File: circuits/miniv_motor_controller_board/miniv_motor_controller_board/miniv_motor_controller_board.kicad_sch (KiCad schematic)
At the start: 5 parts, among them U1 Teensy4.1, U2 NSL-32

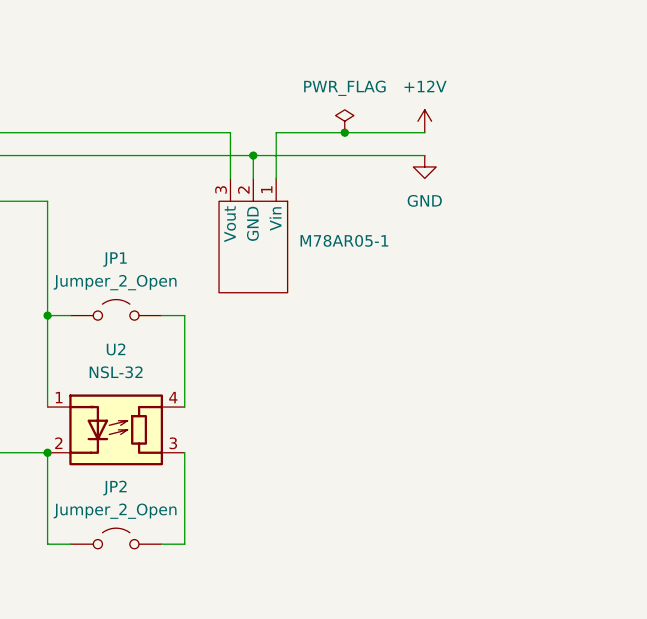
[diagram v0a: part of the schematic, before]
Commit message: add connectors
Signed-off-by: Masaya Kataoka <ms.kataoka@gmail.com>
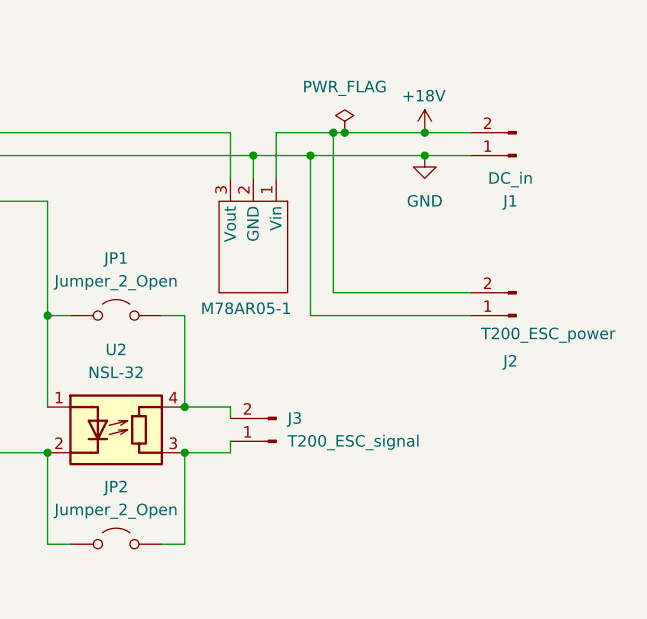
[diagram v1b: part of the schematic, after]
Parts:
- added J1: DC_in, symbol Connector:Conn_01x02_Pin
- added J2: T200_ESC_power, symbol Connector:Conn_01x02_Pin
- added J3: T200_ESC_signal, symbol Connector:Conn_01x02_Pin
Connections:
- net GND: now also J1.1 (Pin_1), J2.1 (Pin_1)
- net at JP1.2 (B), U2.4 (R): now also J3.2 (Pin_2)
- net at JP2.2 (B), U2.3 (R): now also J3.1 (Pin_1)
- net +12V renamed +18V
- net +18V: now also J1.2 (Pin_2), J2.2 (Pin_2)

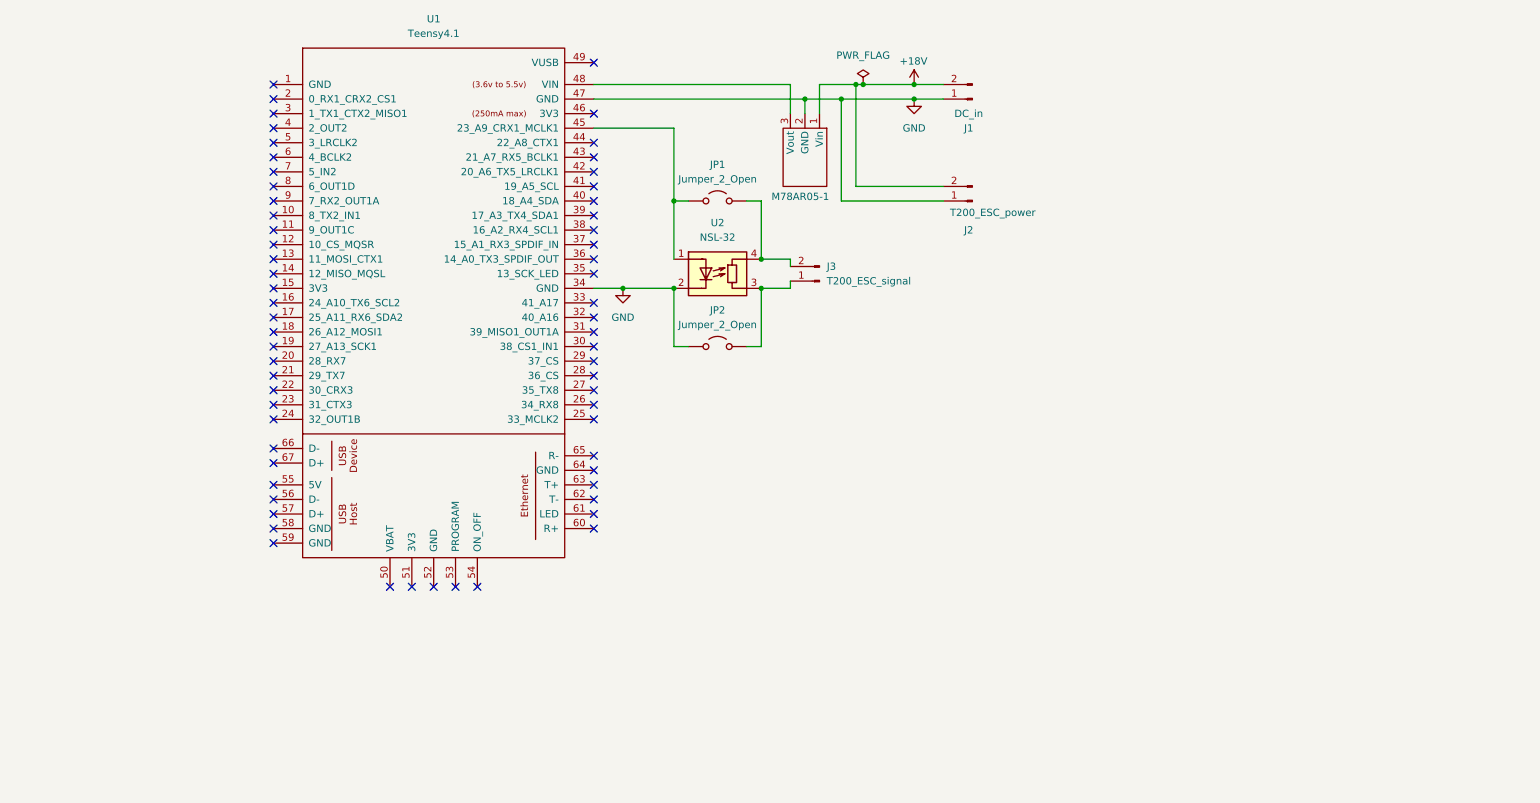
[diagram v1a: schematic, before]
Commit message: add some footprint
Signed-off-by: Masaya Kataoka <ms.kataoka@gmail.com>
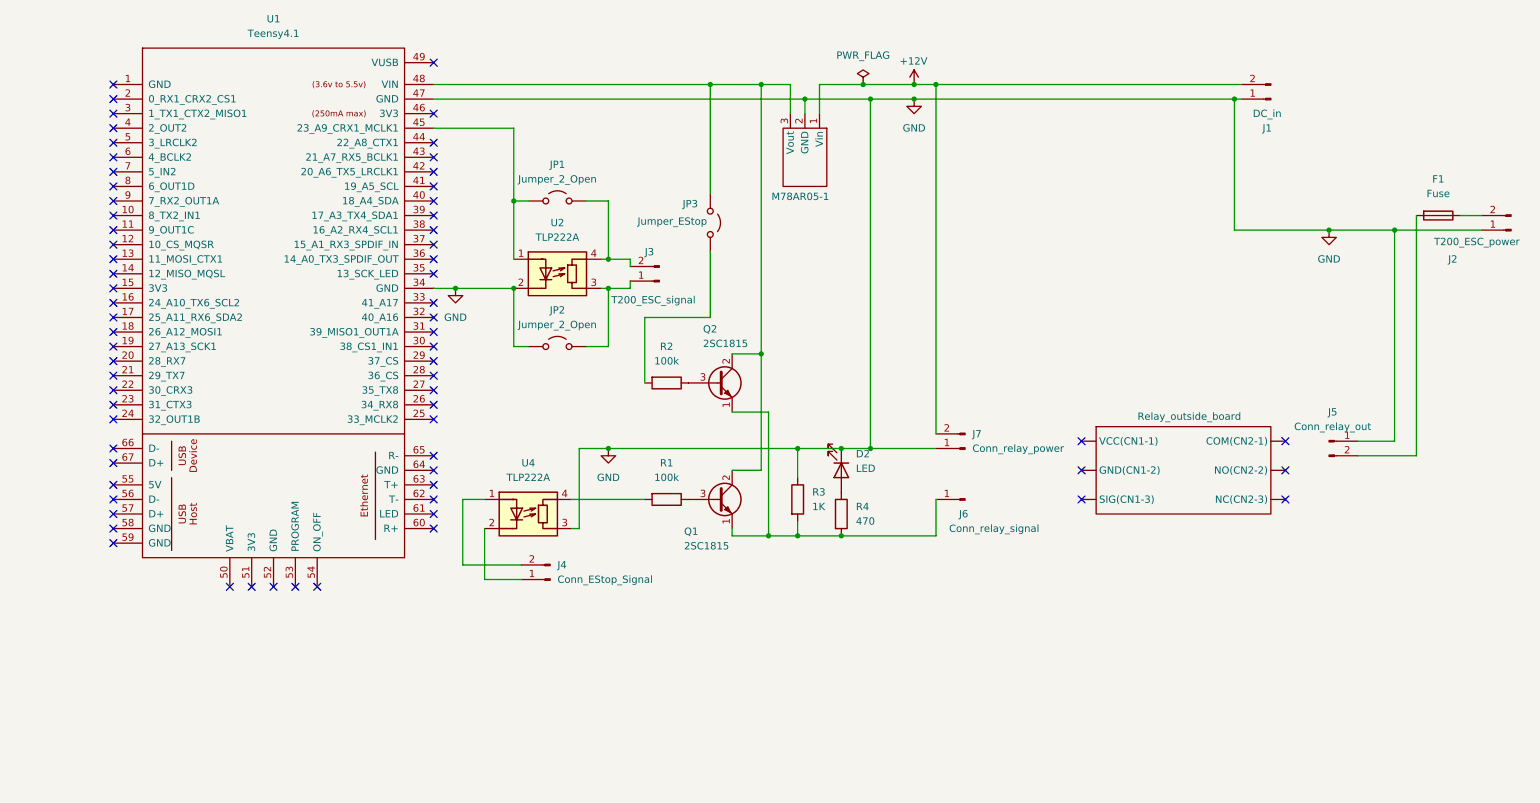
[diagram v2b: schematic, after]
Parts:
- added D2: LED, LED_THT:LED_D3.0mm, symbol Device:LED
- added F1: Fuse, 3557-15:3557-15, symbol Device:Fuse
- added J4: Conn_EStop_Signal, Connector_AMASS:AMASS_XT30PW-F_1x02_P2.50mm_Horizontal, symbol Connector:Conn_01x02_Pin
- added J5: Conn_relay_out, symbol Connector:Conn_01x02_Pin
- added J6: Conn_relay_signal, symbol Connector:Conn_01x01_Pin
- added J7: Conn_relay_power, symbol Connector:Conn_01x02_Pin
- added JP3: Jumper_EStop, Connector_PinHeader_2.54mm:PinHeader_1x02_P2.54mm_Vertical, symbol Jumper:Jumper_2_Open
- added Q1, Q2: 2SC1815, Package_TO_SOT_THT:TO-92_Inline, symbol Transistor_BJT:2SC1815
- added R1, R2: 100k, Resistor_THT:R_Axial_DIN0207_L6.3mm_D2.5mm_P10.16mm_Horizontal, symbol Device:R
- added R3: 1K, Resistor_THT:R_Axial_DIN0207_L6.3mm_D2.5mm_P10.16mm_Horizontal, symbol Device:R
- added R4: 470, Resistor_THT:R_Axial_DIN0207_L6.3mm_D2.5mm_P10.16mm_Horizontal, symbol Device:R
- added Relay_outside_board: ~, symbol AE-RELAY953B-12V:AE-RELAY953B-12V
- added U4: TLP222A, Package_DIP:DIP-4_W7.62mm, symbol Isolator:NSL-32
- J1, J2: footprint (none) -> Connector_AMASS:AMASS_XT30PW-F_1x02_P2.50mm_Horizontal
- JP1, JP2: footprint (none) -> Connector_PinHeader_2.54mm:PinHeader_1x02_P2.54mm_Vertical
- U1: footprint (none) -> Teensy:Teensy41
- U2: value NSL-32 -> TLP222A; footprint OptoDevice:Luna_NSL-32 -> Package_DIP:DIP-4_W7.62mm
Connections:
- net GND: now also D2.1 (K), J5.1 (Pin_1), J7.1 (Pin_1), R3.1, U4.3 (R)
- net at M78AR05-1.3 (Vout), U1.48 (VIN): now also JP3.1 (A), Q1.2 (C), Q2.2 (C)
- net +18V renamed +12V
- net +12V: now also J7.2 (Pin_2); no longer J2.2 (Pin_2)
- new net: J6.1 (Pin_1), Q1.1 (E), Q2.1 (E), R3.2, R4.2
- new net: D2.2 (A), R4.1
- new net: Q2.3 (B), R2.1
- new net: JP3.2 (B), R2.2
- new net: F1.1, J2.2 (Pin_2)
- new net: F1.2, J5.2 (Pin_2)
- new net: Q1.3 (B), R1.1
- new net: J4.1 (Pin_1), U4.2 (K)
- new net: J4.2 (Pin_2), U4.1 (A)
- new net: R1.2, U4.4 (R)
- no-connect marks 63 -> 69
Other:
- moved on the sheet: J1, J2, J3, JP1, JP2, U1, U2

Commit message: update connection
Signed-off-by: Masaya Kataoka <ms.kataoka@gmail.com>
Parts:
- removed J5: Conn_relay_out, symbol Connector:Conn_01x02_Pin
- removed J6: Conn_relay_signal, symbol Connector:Conn_01x01_Pin
- removed J7: Conn_relay_power, symbol Connector:Conn_01x02_Pin
- removed U2, U4: TLP222A, Package_DIP:DIP-4_W7.62mm, symbol Isolator:NSL-32
- added JP4, JP5, JP6: Jumper_2_Bridged, Connector_Wire:SolderWire-0.1sqmm_1x01_D0.4mm_OD1mm, symbol Jumper:Jumper_2_Bridged
- added JP7, JP8: Jumper_2_Bridged, Connector_Wire:SolderWire-0.5sqmm_1x01_D0.9mm_OD2.1mm, symbol Jumper:Jumper_2_Bridged
- added U2, U3: TLP222A, Package_DIP:DIP-4_W7.62mm, symbol Relay_SolidState:TLP222A
- renumbered Relay_outside_board to U4
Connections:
- net +12V: now also JP6.1 (A)
- net GND: now also JP5.1 (A), JP8.2 (B), U2.2
- net at JP1.1 (A), U1.45 (23_A9_CRX1_MCLK1): now also U2.1
- net at J3.2 (Pin_2), JP1.2 (B): now also U2.4
- net at Q1.1 (E), Q2.1 (E), R3.2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: now also JP4.1 (A)
- net at JP3.2 (B), R2.2: now also U3.4
- net at J3.1 (Pin_1), JP2.2 (B): now also U2.3
- net at F1.2: now also JP7.2 (B)
- net at U4. (VCC(CN1-1)): now also JP7.1 (A)
- net at J4.1 (Pin_1): now also U3.2
- net at J4.2 (Pin_2): now also U3.1
- net at R1.2: now also U3.3
- new net: JP8.1 (A), U4. (VCC(CN1-1))
- new net: JP5.2 (B), U4. (VCC(CN1-1))
- new net: JP6.2 (B), U4. (VCC(CN1-1))
- new net: JP4.2 (B), U4. (VCC(CN1-1))
- no-connect marks 69 -> 64
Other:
- moved on the sheet: U4

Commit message: modify resister
Signed-off-by: Masaya Kataoka <ms.kataoka@gmail.com>
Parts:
- removed JP2: Jumper_2_Open, Connector_PinHeader_2.54mm:PinHeader_1x02_P2.54mm_Vertical, symbol Jumper:Jumper_2_Open
- added R5: 390, Resistor_THT:R_Axial_DIN0207_L6.3mm_D2.5mm_P10.16mm_Horizontal, symbol Device:R
- added R6: 1K, Resistor_THT:R_Axial_DIN0207_L6.3mm_D2.5mm_P10.16mm_Horizontal, symbol Device:R
- J3: footprint (none) -> Connector_AMASS:AMASS_XT30PW-F_1x02_P2.50mm_Horizontal
- M78AR05-1: footprint (none) -> M78AR05-1:M78AR05-1
- U2, U3: value TLP222A -> TLP624
- U4: footprint (none) -> AE-RELAY953B-12V:AE-RELAY953B-12V
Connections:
- net GND: now also J3.1 (Pin_1), U2.3
- net at JP1.1 (A), U1.45 (23_A9_CRX1_MCLK1): now also R6.1; no longer U2.1
- net at U4. (VCC(CN1-1)): now also JP7.1 (A)
- new net: R5.2, U2.1
- new net: R5.1, R6.2
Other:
- moved on the sheet: JP1, JP4, JP5, JP6, JP7, JP8

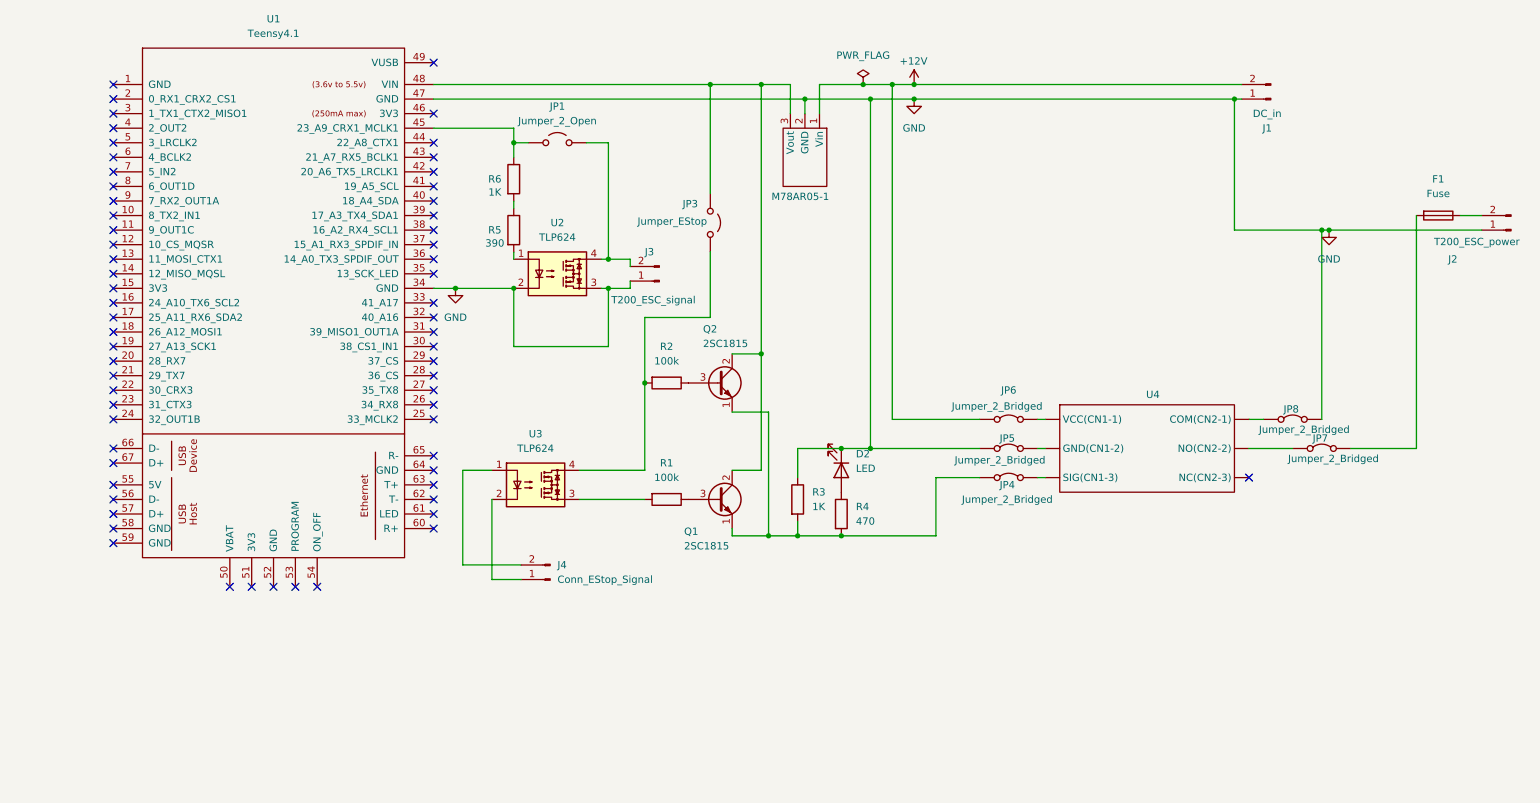
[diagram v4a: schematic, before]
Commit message: fix connection
Signed-off-by: Masaya Kataoka <ms.kataoka@gmail.com>
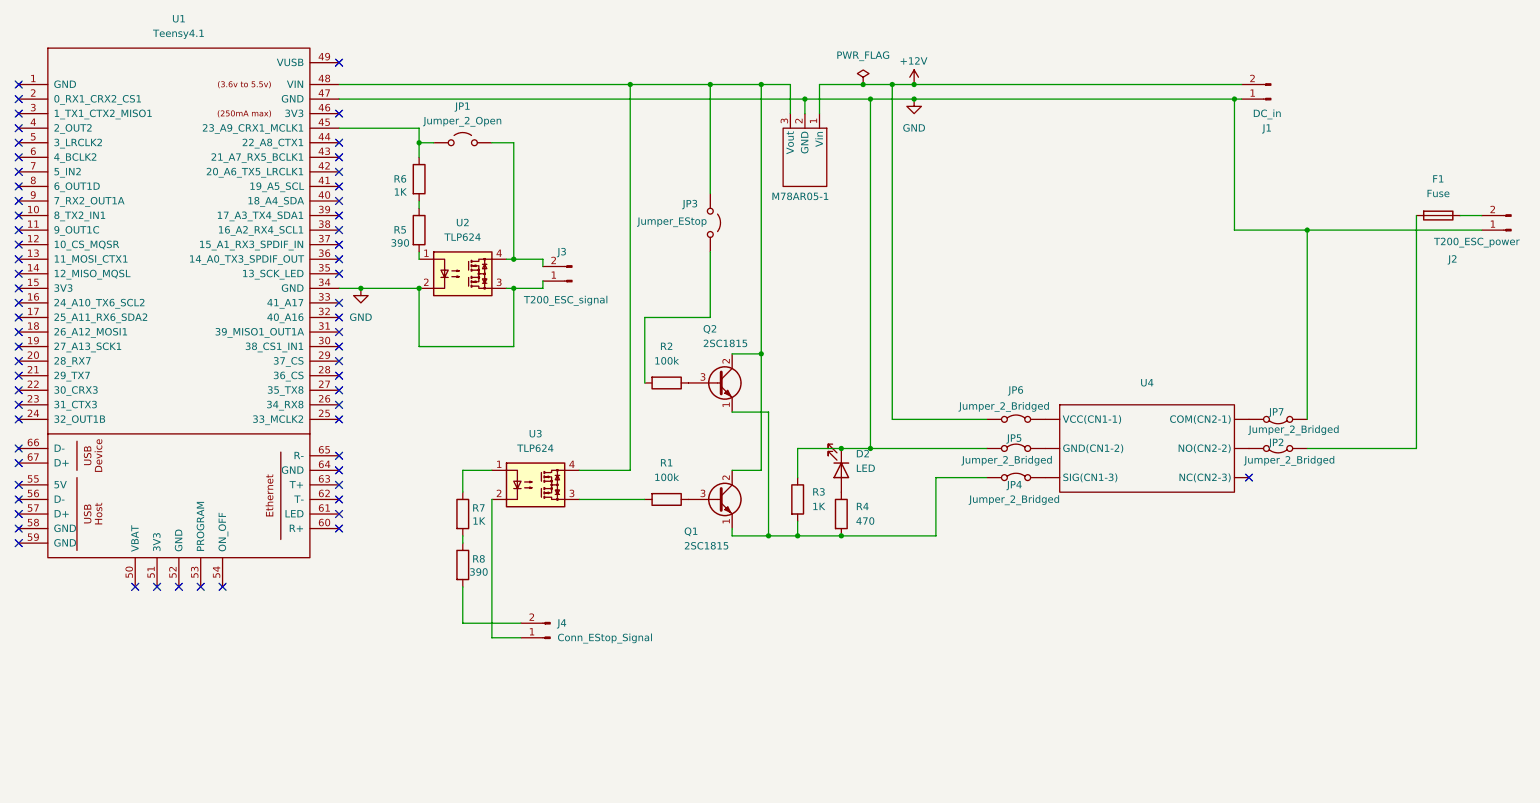
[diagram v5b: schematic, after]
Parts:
- removed JP8: Jumper_2_Bridged, Connector_Wire:SolderWire-0.5sqmm_1x01_D0.9mm_OD2.1mm, symbol Jumper:Jumper_2_Bridged
- added JP2: Jumper_2_Bridged, Connector_Wire:SolderWire-0.5sqmm_1x01_D0.9mm_OD2.1mm, symbol Jumper:Jumper_2_Bridged
- added R7: 1K, Resistor_THT:R_Axial_DIN0207_L6.3mm_D2.5mm_P10.16mm_Horizontal, symbol Device:R
- added R8: 390, Resistor_THT:R_Axial_DIN0207_L6.3mm_D2.5mm_P10.16mm_Horizontal, symbol Device:R
- U4: footprint AE-RELAY953B-12V:AE-RELAY953B-12V -> (none)
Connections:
- net GND: now also JP7.1 (A)
- net at U4. (VCC(CN1-1)): now also JP2.2 (B)
- net at JP3.1 (A), M78AR05-1.3 (Vout), Q1.2 (C)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: now also U3.4
- net at JP3.2 (B), R2.2: no longer U3.4
- net at JP7.2 (B): now also U4. (VCC(CN1-1)); no longer F1.2
- net at U3.1: now also R7.1; no longer J4.2 (Pin_2)
- new net: R7.2, R8.1
- new net: J4.2 (Pin_2), R8.2
- new net: F1.2, JP2.1 (A)
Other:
- moved on the sheet: J3, J4, JP1, JP4, JP5, JP6, R5, R6, U1, U2

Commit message: update text
Signed-off-by: Masaya Kataoka <ms.kataoka@gmail.com>
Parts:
- JP2: value Jumper_2_Bridged -> Relay_NO
- JP4: value Jumper_2_Bridged -> Relay_SIG
- JP5: value Jumper_2_Bridged -> Relay_GND
- JP6: value Jumper_2_Bridged -> Relay_VCC
- JP7: value Jumper_2_Bridged -> Relay_COM
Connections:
- net at U4. (VCC(CN1-1)): now also JP2.2 (B)
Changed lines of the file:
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@@
 			)
 		)
-		(property "Value" "Jumper_2_Bridged"
+		(property "Value" "Relay_GND"
 			(at 194.056 130.302 0)
 			(effects
@@
 			)
 		)
-		(property "Value" "Jumper_2_Bridged"
+		(property "Value" "Relay_COM"
 			(at 244.094 124.968 0)
 			(effects
@@
 			)
 		)
-		(property "Value" "Jumper_2_Bridged"
+		(property "Value" "Relay_VCC"
 			(at 193.548 120.904 0)
 			(effects
@@
 			)
 		)
-		(property "Value" "Jumper_2_Bridged"
+		(property "Value" "Relay_SIG"
 			(at 195.326 137.16 0)
 			(effects
@@
 			)
 		)
-		(property "Value" "Jumper_2_Bridged"
+		(property "Value" "Relay_NO"
 			(at 243.332 130.302 0)
 			(effects

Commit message: add hole
Signed-off-by: Masaya Kataoka <ms.kataoka@gmail.com>
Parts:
- added H1, H2, H3, H4: MountingHole, MountingHole:MountingHole_3.2mm_M3, symbol Mechanical:MountingHole
- J1, J2: footprint Connector_AMASS:AMASS_XT30PW-F_1x02_P2.50mm_Horizontal -> Connector_AMASS:AMASS_XT60PW-F_1x02_P7.20mm_Horizontal
- J4: footprint Connector_AMASS:AMASS_XT30PW-F_1x02_P2.50mm_Horizontal -> Connector_JST:JST_XH_B2B-XH-A_1x02_P2.50mm_Vertical
- JP3: value Jumper_EStop -> Disable_EStop
- U4: footprint (none) -> AE-RELAY953B-12V:AE-RELAY953B-12V
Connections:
- net +12V: now also JP7.1 (A)
- net GND: no longer JP7.1 (A)
- net at U4. (VCC(CN1-1)): now also JP2.2 (B)
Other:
- moved on the sheet: J1

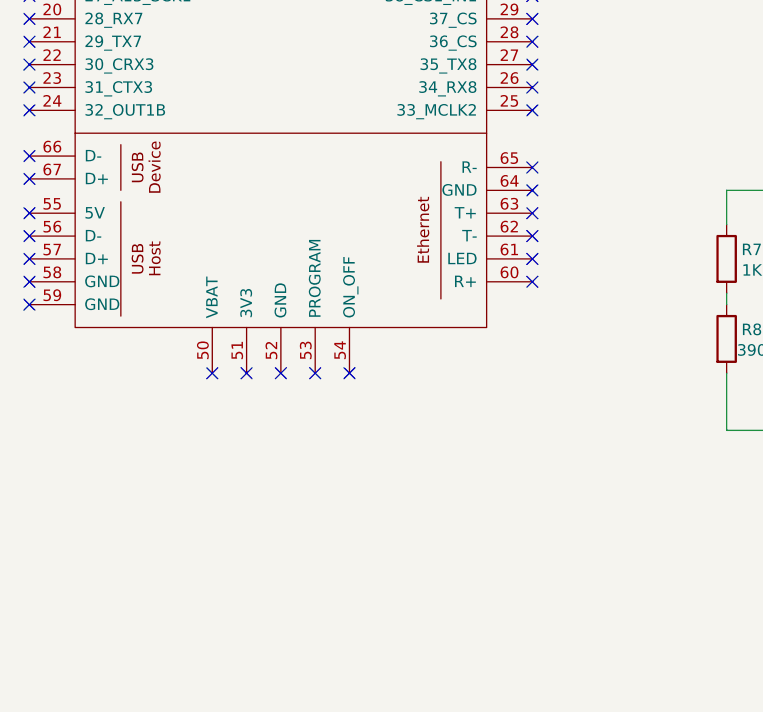
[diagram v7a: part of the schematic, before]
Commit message: add RJ45 connector
Signed-off-by: Masaya Kataoka <ms.kataoka@gmail.com>
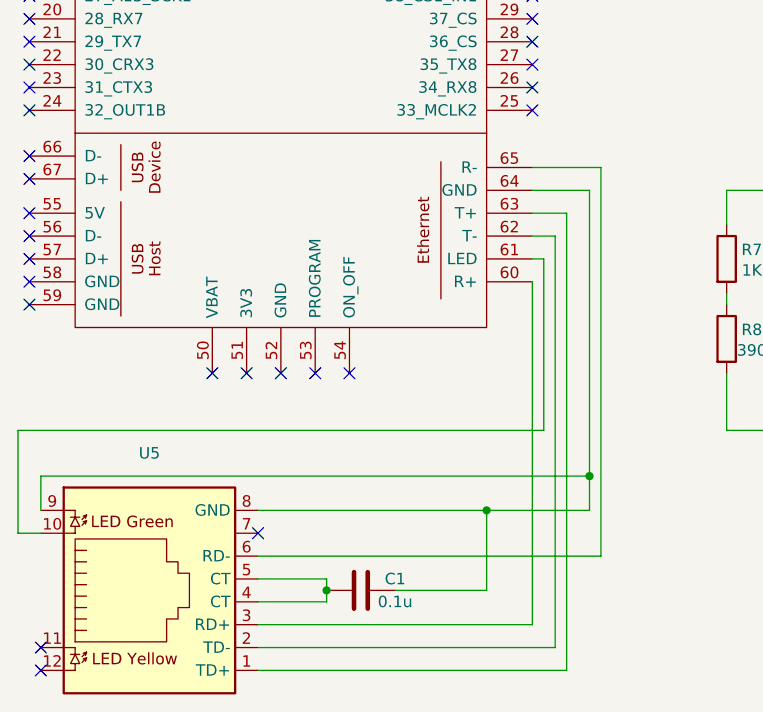
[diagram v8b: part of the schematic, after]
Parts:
- added C1: 0.1u, symbol Device:C
- added U5: ~, https://akizukidenshi.com/catalog/g/g129472/, symbol RJLD-260YC1:RJLD-260YC1
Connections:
- net at U4. (VCC(CN1-1)): now also JP2.2 (B)
- net at U1.60 (R+): now also U5.3 (RD+)
- net at U1.61 (LED): now also U5.10
- net at U1.62 (T-): now also U5.2 (TD-)
- net at U1.63 (T+): now also U5.1 (TD+)
- net at U1.64 (GND): now also C1.1, U5.8 (GND), U5.9
- net at U1.65 (R-): now also U5.6 (RD-)
- new net: C1.2, U5.4 (CT), U5.5 (CT)
- no-connect marks 64 -> 61
